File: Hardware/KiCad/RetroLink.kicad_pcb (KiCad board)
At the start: 2 copper layers, 154 x 91 mm, 90 parts, among them CON1 HSMM-A100-S00J1, IC1 TLV320AIC1110PBS, IC12 BQ24090DGQR, IC2 IIC 0x3A MAX7329AWE+T, IC3 BC846AW-7-F, IC6 MCP1642B-50I_MS, IC7 IIC 0x38 MAX7329AWE+T, IC8 MAX40200AUK+T, J10 SAMTEC-HMTSW-101-24-X-S-290, J11 SAMTEC-HMTSW-101-24-X-S-290, J12 SAMTEC-HMTSW-101-24-X-S-290, J2 95501-2641, J21 PJS008-2120-0, J28 SAMTEC-HMTSW-101-24-X-S-290, Q1 BSS138, Q2 BSS138, U1 Ag1170-S5, U3 IIC 0x3C DM-OLED096-636, U5 1043

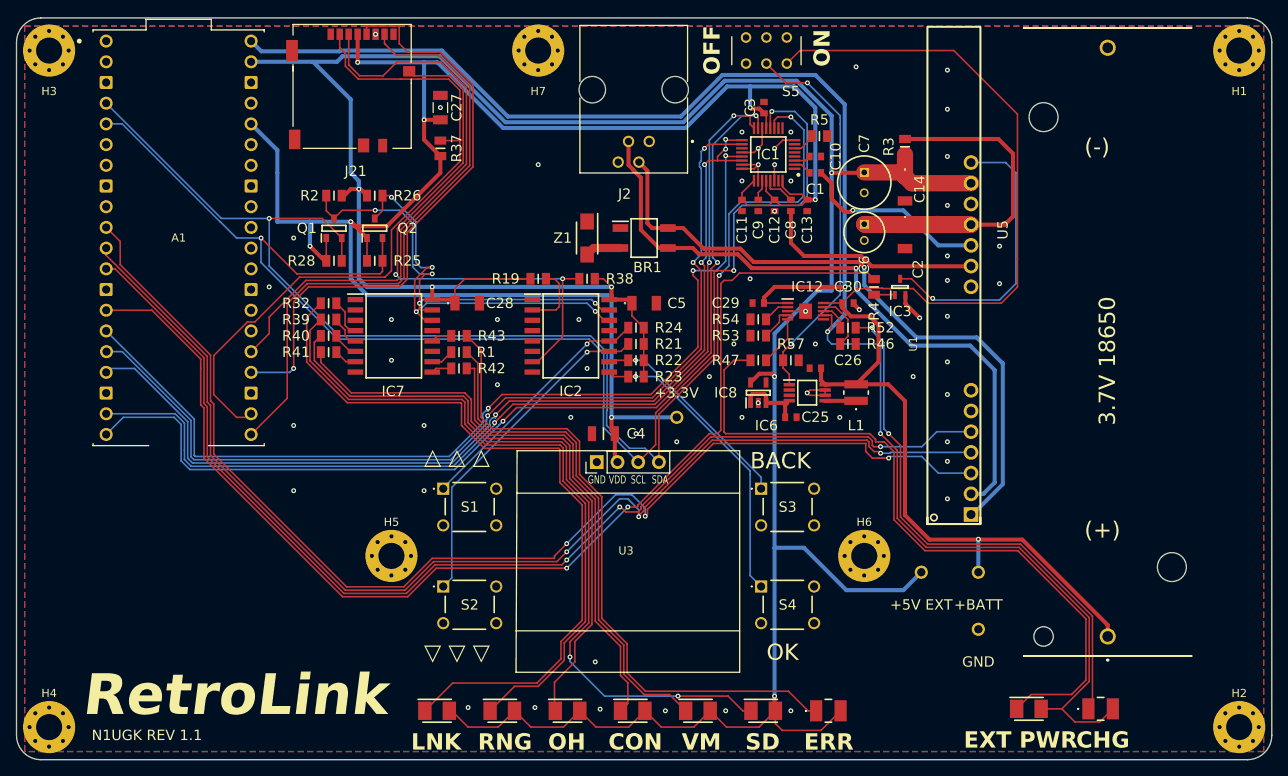
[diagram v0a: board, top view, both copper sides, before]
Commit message: Fix for swhook signal
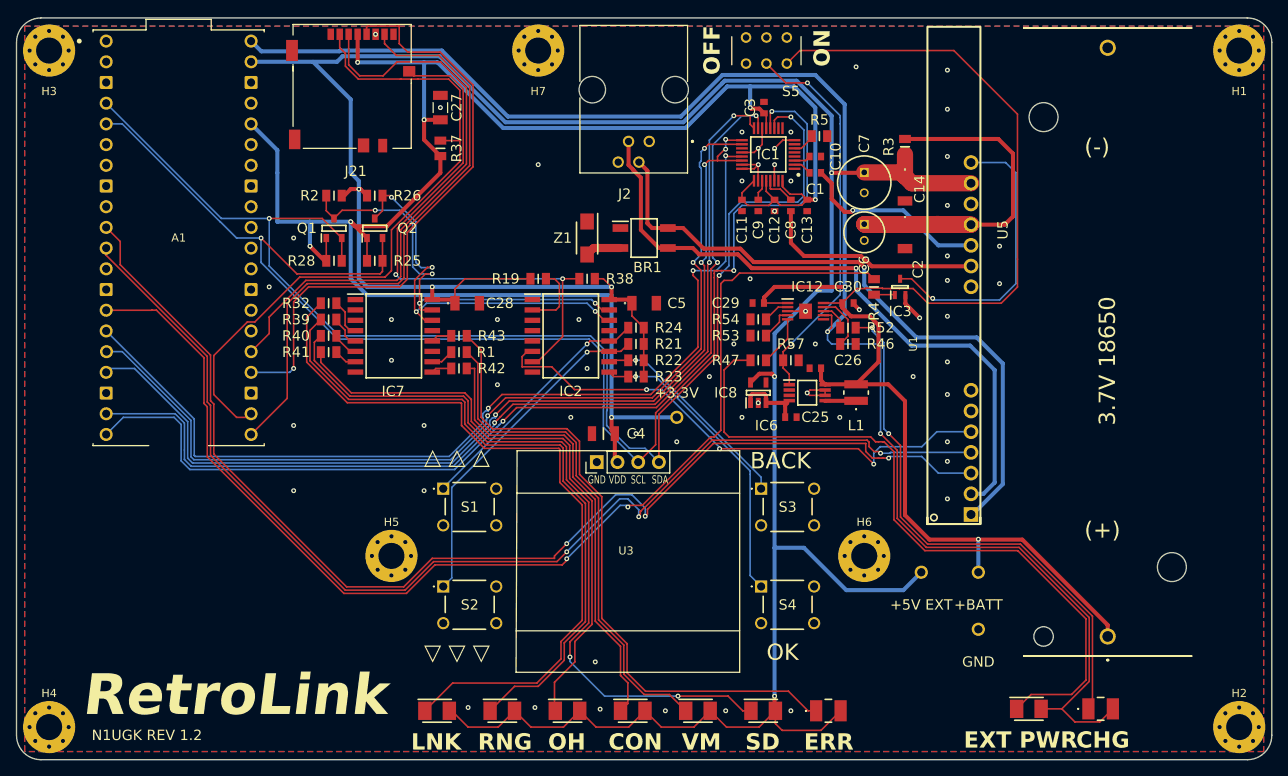
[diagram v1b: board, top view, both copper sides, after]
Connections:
- IC2 pad 6: unconnected-(IC2-P2-Pad6) -> /SWHOOK
- U1 pad 5: /GPIO_9 -> /SWHOOK
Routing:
- net /GPIO_9: track 139.7 -> 0.00 mm, vias 3 -> 0
- net /SWHOOK: track 0.00 -> 65.3 mm, vias 0 -> 3
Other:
- board text added: "N1UGK REV 1.2"
- board text removed: "N1UGK REV 1.1"

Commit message: audio cutout fixes, number lookup, misc updates
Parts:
- added R6: 22K, footprints:RESC2013X65N, F.Cu at (129.9, 59.6)
- added R7: 10K, footprints:RESC2013X65N, F.Cu at (133.3, 58.9)
- added R8: 22K, footprints:RESC2013X65N, F.Cu at (140.8, 41.8)
- added R9: 10K, footprints:RESC2013X65N, F.Cu at (143.1, 41.8)
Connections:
- C1 pad 2: Net-(U1-VOUT) -> Net-(C1-Pad2)
- C8 pad 2: Net-(U1-VIN) -> Net-(C8-Pad2)
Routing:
- net Net-(C1-Pad2): track 0.00 -> 11.6 mm
- net Net-(U1-VIN): track 27.1 -> 20.8 mm
- net Net-(C8-Pad2): track 0.00 -> 5.10 mm
- net Net-(U1-VOUT): track 23.4 -> 26.5 mm

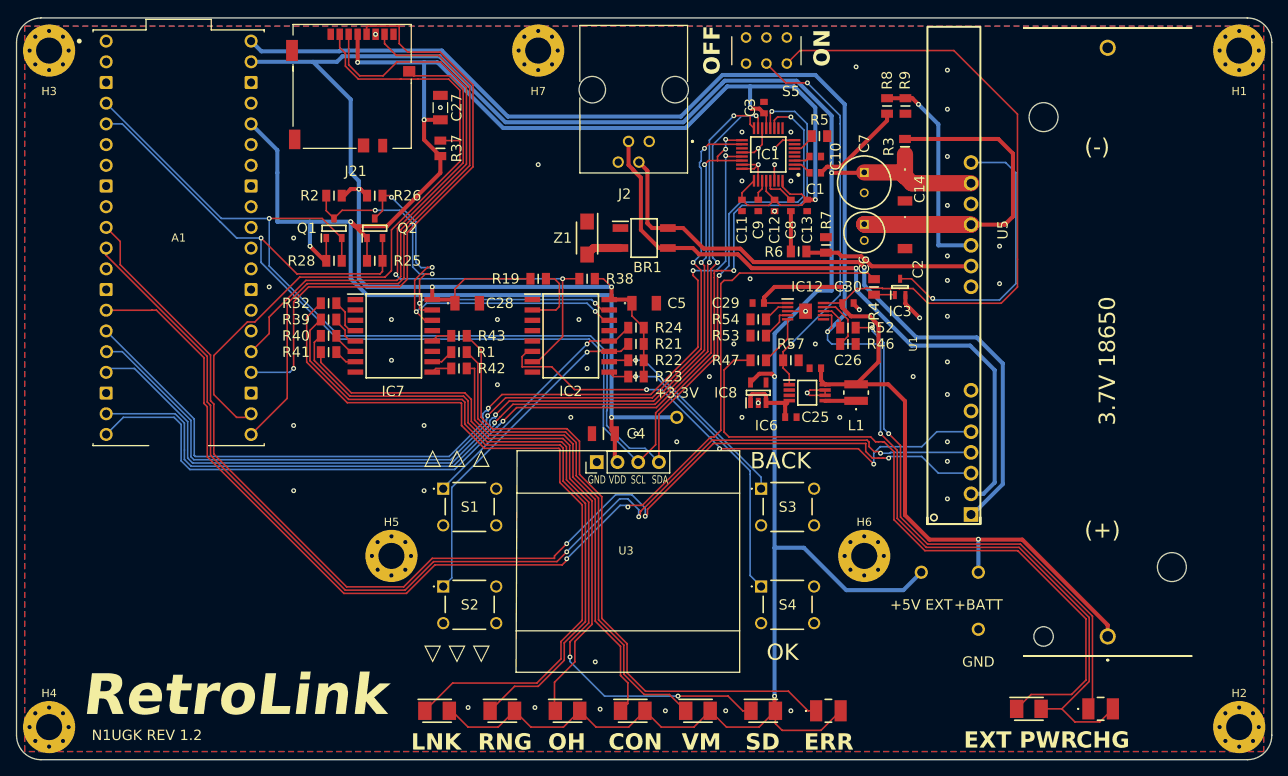
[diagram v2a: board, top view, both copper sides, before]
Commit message: fixes to audio levels and gpio outputs
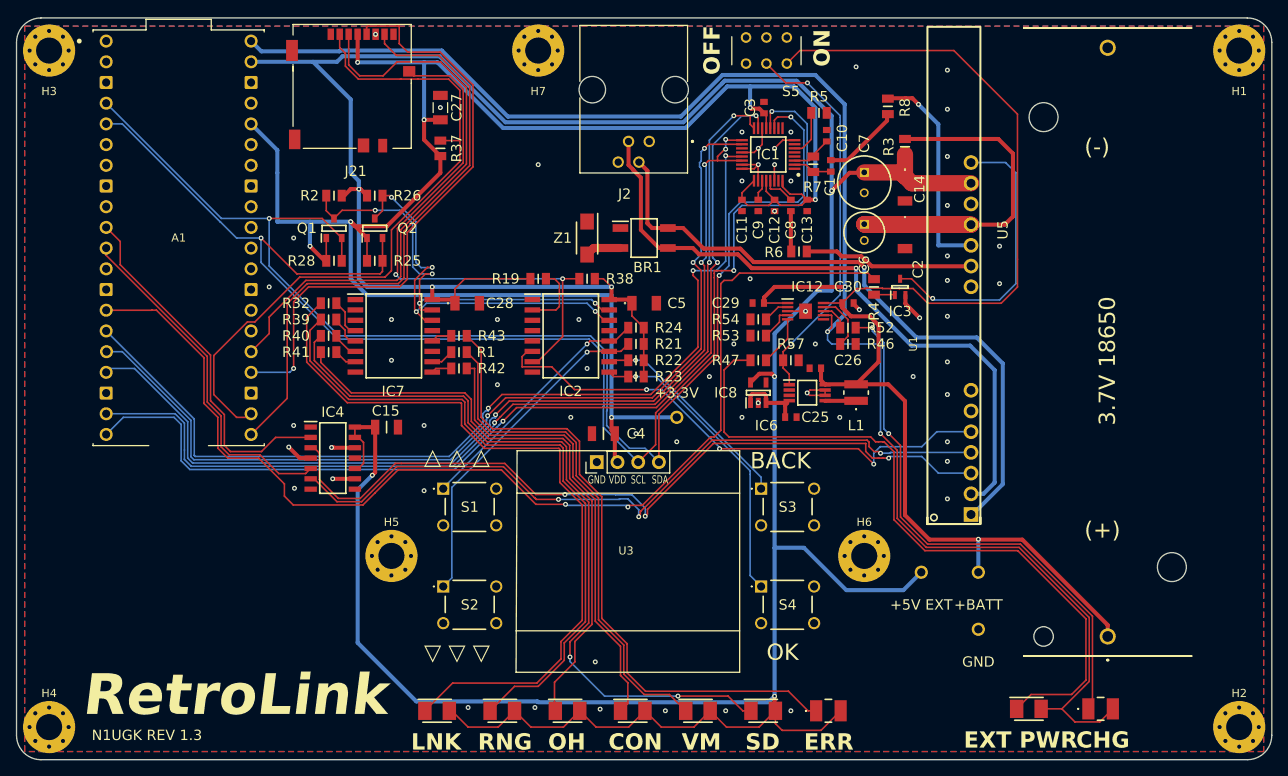
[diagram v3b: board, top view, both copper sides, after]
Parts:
- removed R9: 10K, footprints:RESC2013X65N
- added C15: 0.1uF, footprints:CAPC3216X229N, F.Cu at (79.4, 81.2)
- added IC4: SN74AHCT125DR, footprints:SOIC127P600X175-14N, F.Cu at (72.8, 85.0)
- R6: value 22K -> 0K
- R7: value 10K -> 8.2K
- R8: value 22K -> 47K
- moved R7 10.0 mm to (131.8, 49.0)
- moved C10 2.91 mm to (133.4, 45.5), turned to -90 degrees
- moved R5 2.85 mm to (132.4, 42.6)
- moved C1 2.08 mm to (133.9, 49.1), turned to 90 degrees
- moved R8 0.11 mm to (140.9, 41.9)
- moved R6 0.05 mm to (130.0, 59.6)
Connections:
- R7 pad 1: Net-(U1-VIN) -> Net-(IC1-MIC1P)
- R7 pad 2: GND -> Net-(IC1-MIC1N)
- U1 pad 3: /GPIO_7 -> /SLIC_FR
- U1 pad 4: /GPIO_8 -> /SLIC_RM
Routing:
- net /GPIO_7: track 145.9 -> 44.4 mm, vias 3 -> 0
- net /GPIO_8: track 141.9 -> 42.8 mm, vias 3 -> 0
- net /SLIC_FR: track 0.00 -> 97.0 mm, vias 0 -> 3
- net /SLIC_RM: track 0.00 -> 92.0 mm, vias 0 -> 3
- net +5V: track 356.8 -> 448.5 mm, vias 6 -> 7
- net GND: track 28.1 -> 36.9 mm, vias 61 -> 64
- net /GPIO_10: track 142.9 -> 137.1 mm
- net Net-(IC1-MIC1N): track 2.06 -> 5.04 mm
- net /CODEC_REXT: track 2.85 -> 5.76 mm
- net Net-(IC1-MIC1P): track 2.26 -> 4.84 mm
- net Net-(C1-Pad2): track 11.6 -> 9.76 mm
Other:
- board text added: "N1UGK REV 1.3"
- board text removed: "N1UGK REV 1.2"
